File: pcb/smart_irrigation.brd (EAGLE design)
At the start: 76.2 x 76.2 mm, 33 parts, among them IC1 TMP36, IC2 7805DT, IC3 7833DT, IC4 DS1307, Q1 IRF730, Q2 32.768, T1 2N3904, U1 BL600

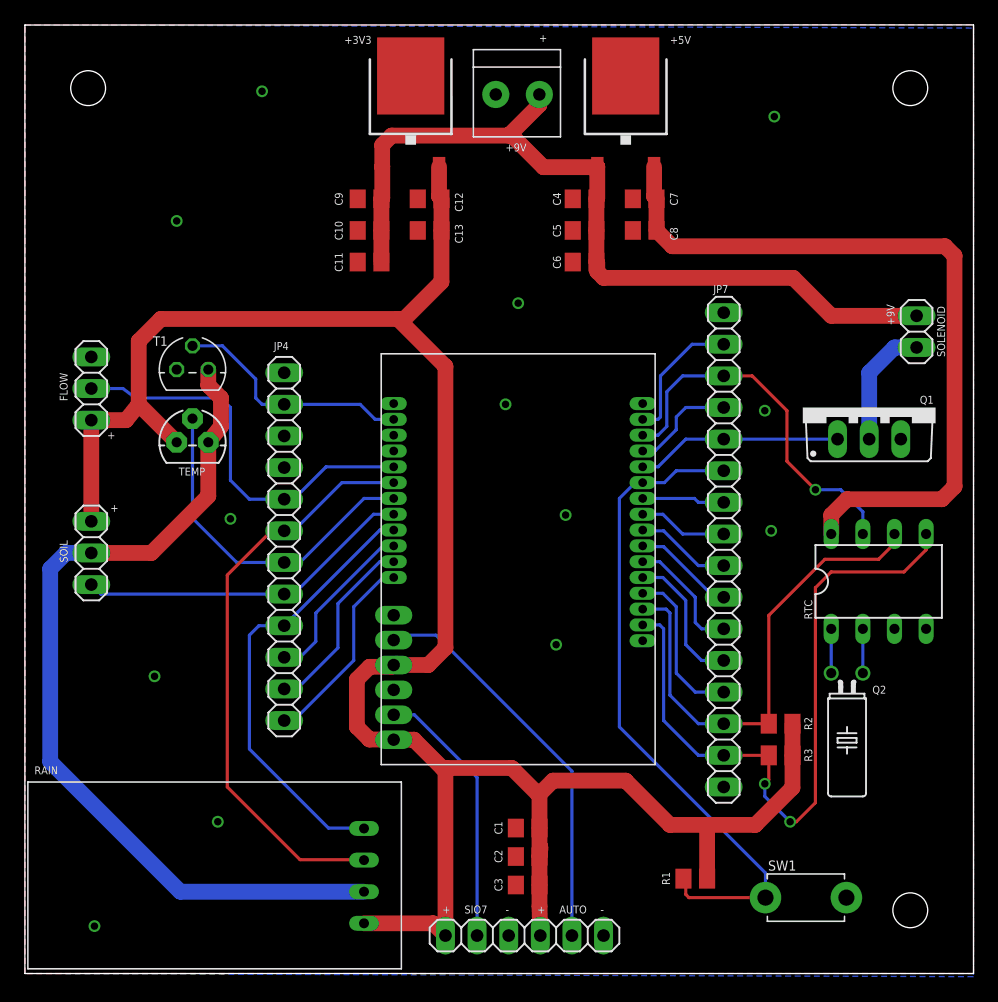
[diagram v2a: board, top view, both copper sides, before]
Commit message: PCB: Move solenoid terminal block away from MOSFET
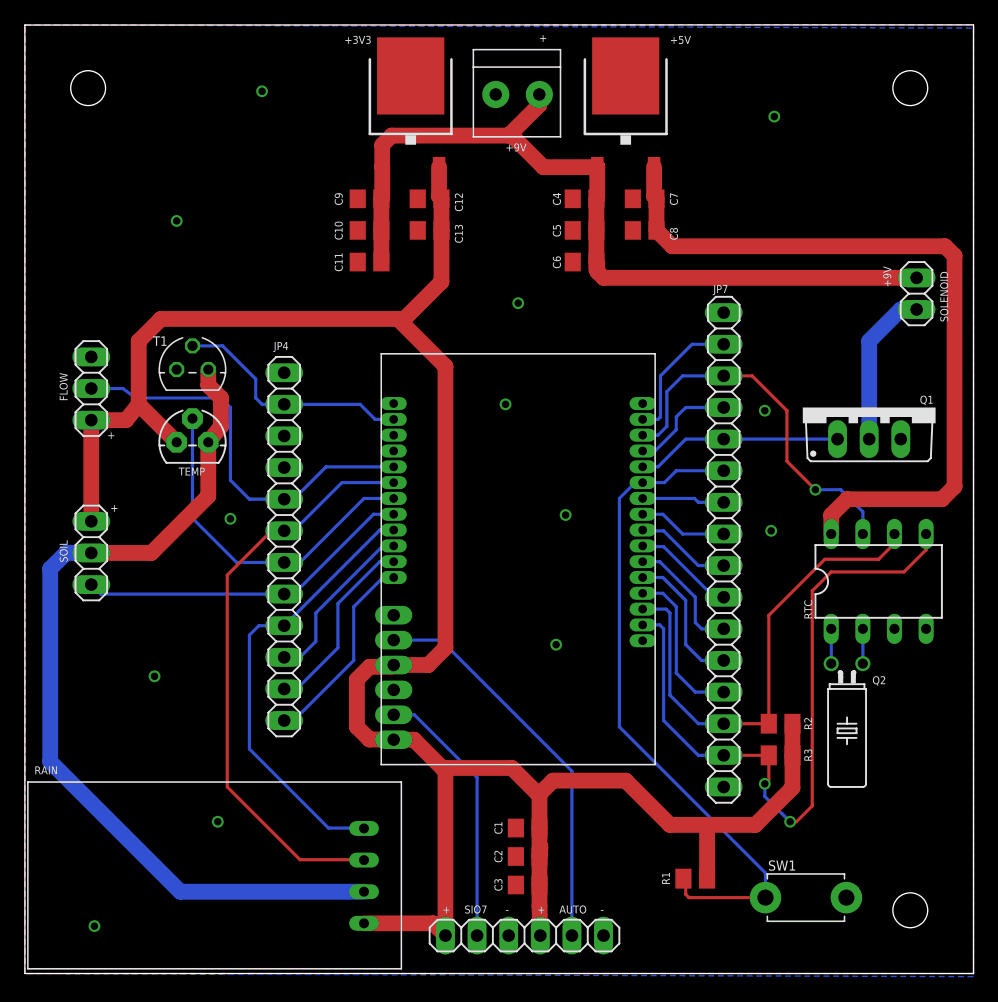
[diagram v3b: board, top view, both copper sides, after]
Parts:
- moved JP8 3.05 mm to (71.6, 54.6)
- moved Q2 0.76 mm to (66.0, 24.9)
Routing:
- net SOL_DRAIN: track 9.99 -> 12.7 mm
- net +9V: track 68.0 -> 66.7 mm
- net N$3: track 3.56 -> 2.79 mm
- net N$1: track 3.56 -> 2.79 mm
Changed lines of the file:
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@@
 <text x="46.228" y="4.826" size="0.635" layer="25" font="vector" ratio="20">-</text>
 <text x="63.246" y="28.448" size="0.635" layer="25" font="vector" ratio="20" rot="R90">RTC</text>
-<text x="73.914" y="49.53" size="0.635" layer="25" font="vector" ratio="20" rot="R90">SOLENOID</text>
-<text x="69.85" y="52.07" size="0.635" layer="25" font="vector" ratio="20" rot="R90">+9V</text>
+<text x="74.168" y="52.324" size="0.635" layer="25" font="vector" ratio="20" rot="R90">SOLENOID</text>
+<text x="69.596" y="55.118" size="0.635" layer="25" font="vector" ratio="20" rot="R90">+9V</text>
 <text x="25.654" y="74.676" size="0.635" layer="25" font="vector" ratio="20">+3V3</text>
 <text x="51.816" y="74.676" size="0.635" layer="25" font="vector" ratio="20">+5V</text>
@@
 </element>
 <element name="IC4" library="adafruit" package="DIL08" value="DS1307" x="68.58" y="31.496" smashed="yes"/>
-<element name="Q2" library="crystal" package="TC38H" value="32.768" x="66.04" y="24.13" smashed="yes" rot="R180">
-<attribute name="MPN" value="" x="66.04" y="24.13" size="1.778" layer="27" rot="R180" display="off"/>
-<attribute name="OC_NEWARK" value="unknown" x="66.04" y="24.13" size="1.778" layer="27" rot="R180" display="off"/>
-<attribute name="OC_FARNELL" value="unknown" x="66.04" y="24.13" size="1.778" layer="27" rot="R180" display="off"/>
-<attribute name="MF" value="" x="66.04" y="24.13" size="1.778" layer="27" rot="R180" display="off"/>
-<attribute name="NAME" x="68.072" y="22.479" size="0.635" layer="25" font="vector" ratio="20"/>
+<element name="Q2" library="crystal" package="TC38H" value="32.768" x="66.04" y="24.892" smashed="yes" rot="R180">
+<attribute name="MPN" value="" x="66.04" y="24.892" size="1.778" layer="27" rot="R180" display="off"/>
+<attribute name="OC_NEWARK" value="unknown" x="66.04" y="24.892" size="1.778" layer="27" rot="R180" display="off"/>
+<attribute name="OC_FARNELL" value="unknown" x="66.04" y="24.892" size="1.778" layer="27" rot="R180" display="off"/>
+<attribute name="MF" value="" x="66.04" y="24.892" size="1.778" layer="27" rot="R180" display="off"/>
+<attribute name="NAME" x="68.072" y="23.241" size="0.635" layer="25" font="vector" ratio="20"/>
 </element>
 <element name="R3" library="rcl" package="M0805" value="2.2k" x="60.706" y="17.526" smashed="yes">
@@
 <attribute name="NAME" x="71.882" y="45.7708" size="0.635" layer="25" font="vector" ratio="20"/>
 </element>
-<element name="JP8" library="pinhead" package="1X02" value="" x="71.628" y="51.562" smashed="yes" rot="R270">
-<attribute name="VALUE" x="68.453" y="54.102" size="1.27" layer="27" rot="R270"/>
+<element name="JP8" library="pinhead" package="1X02" value="" x="71.628" y="54.61" smashed="yes" rot="R270">
+<attribute name="VALUE" x="68.453" y="57.15" size="1.27" layer="27" rot="R270"/>
 </element>
 <element name="T1" library="transistor" package="TO92" value="2N3904" x="13.462" y="48.514" smashed="yes">
@@
 <wire x1="28.708" y1="64.796" x2="28.708" y2="62.302" width="1.27" layer="1"/>
 <wire x1="28.708" y1="62.302" x2="28.636" y2="62.23" width="1.27" layer="1"/>
-<wire x1="71.628" y1="52.832" x2="64.77" y2="52.832" width="1.27" layer="1"/>
-<wire x1="64.77" y1="52.832" x2="61.722" y2="55.88" width="1.27" layer="1"/>
-<wire x1="61.722" y1="55.88" x2="46.482" y2="55.88" width="1.27" layer="1"/>
+<wire x1="71.628" y1="55.88" x2="46.482" y2="55.88" width="1.27" layer="1"/>
 <wire x1="46.482" y1="55.88" x2="45.974" y2="56.388" width="1.27" layer="1"/>
 <wire x1="45.974" y1="56.388" x2="45.974" y2="57.084" width="1.27" layer="1"/>
@@
 <contactref element="U1" pad="J5_2"/>
 <contactref element="JP5" pad="2"/>
-<wire x1="43.942" y1="16.256" x2="33.02" y2="27.178" width="0.254" layer="16"/>
-<wire x1="33.02" y1="27.178" x2="29.804" y2="27.178" width="0.254" layer="16"/>
-<wire x1="29.804" y1="27.178" x2="29.624" y2="26.782" width="0.254" layer="16"/>
 <wire x1="43.942" y1="16.256" x2="43.942" y2="3.048" width="0.254" layer="16"/>
+<wire x1="29.624" y1="26.782" x2="33.416" y2="26.782" width="0.254" layer="16"/>
+<wire x1="33.416" y1="26.782" x2="43.942" y2="16.256" width="0.254" layer="16"/>
 </signal>
 <signal name="SIO_7">
@@
 <wire x1="54.102" y1="20.066" x2="56.134" y2="20.066" width="0.254" layer="16"/>
 <wire x1="69.85" y1="35.4584" x2="69.85" y2="35.306" width="0.254" layer="1"/>
-<wire x1="69.85" y1="35.306" x2="69.85" y2="34.544" width="0.254" layer="1"/>
 <wire x1="69.85" y1="34.544" x2="68.58" y2="33.274" width="0.254" layer="1"/>
 <wire x1="68.58" y1="33.274" x2="64.262" y2="33.274" width="0.254" layer="1"/>
@@
 <wire x1="59.756" y1="20.066" x2="59.756" y2="28.768" width="0.254" layer="1"/>
 <wire x1="59.756" y1="28.768" x2="64.262" y2="33.274" width="0.254" layer="1"/>
+<wire x1="69.85" y1="35.306" x2="69.85" y2="34.544" width="0.254" layer="1"/>
 </signal>
 <signal name="SDA">
@@
 <via x="61.468" y="12.192" extent="1-16" drill="0.6"/>
 <wire x1="61.468" y1="12.192" x2="61.976" y2="12.192" width="0.254" layer="1"/>
-<wire x1="61.976" y1="12.192" x2="63.5" y2="13.716" width="0.254" layer="1"/>
-<wire x1="63.5" y1="13.716" x2="63.5" y2="30.988" width="0.254" layer="1"/>
-<wire x1="63.5" y1="30.988" x2="64.77" y2="32.258" width="0.254" layer="1"/>
+<wire x1="61.976" y1="12.192" x2="63.246" y2="13.462" width="0.254" layer="1"/>
+<wire x1="63.246" y1="13.462" x2="63.246" y2="30.734" width="0.254" layer="1"/>
+<wire x1="63.246" y1="30.734" x2="64.77" y2="32.258" width="0.254" layer="1"/>
 <wire x1="64.77" y1="32.258" x2="70.612" y2="32.258" width="0.254" layer="1"/>
 <wire x1="70.612" y1="32.258" x2="72.39" y2="34.036" width="0.254" layer="1"/>
@@
 <contactref element="JP8" pad="2"/>
 <contactref element="Q1" pad="D"/>
-<wire x1="71.628" y1="50.292" x2="69.85" y2="50.292" width="1.27" layer="16"/>
-<wire x1="69.85" y1="50.292" x2="67.818" y2="48.26" width="1.27" layer="16"/>
-<wire x1="67.818" y1="48.26" x2="67.818" y2="42.926" width="1.27" layer="16"/>
+<wire x1="67.818" y1="50.8" x2="67.818" y2="42.926" width="1.27" layer="16"/>
+<wire x1="67.818" y1="50.8" x2="70.358" y2="53.34" width="1.27" layer="16"/>
+<wire x1="70.358" y1="53.34" x2="71.628" y2="53.34" width="1.27" layer="16"/>
 </signal>
 <signal name="3V3_TRAN_COL">
@@
 <contactref element="Q2" pad="2"/>
 <contactref element="IC4" pad="1"/>
-<wire x1="64.77" y1="27.686" x2="64.77" y2="24.13" width="0.254" layer="16"/>
+<wire x1="64.77" y1="27.686" x2="64.77" y2="24.892" width="0.254" layer="16"/>
 </signal>
 <signal name="N$3">
 <contactref element="Q2" pad="1"/>
 <contactref element="IC4" pad="2"/>
-<wire x1="67.31" y1="27.686" x2="67.31" y2="24.13" width="0.254" layer="16"/>
+<wire x1="67.31" y1="27.686" x2="67.31" y2="24.892" width="0.254" layer="16"/>
 </signal>
 <signal name="SIO_18">
